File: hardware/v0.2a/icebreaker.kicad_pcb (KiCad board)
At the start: 4 copper layers, 73 x 37 mm, 125 parts, among them J1 Jumper, J10 Jumper, J11 Jumper, J12 Jumper, J13 Jumper, J14 Jumper, J15 Jumper, J16 Jumper, J17 Jumper, J18 Jumper, J19 Jumper, J2 Jumper, J20 Flash, J21 PMOD_1A, J22 PMOD_1B, J23 PMOD_2H, J24 PMOD_2P, J25 RGB Led, J26 5V AUX, J27 5V AUX, J3 Jumper, J4 Jumper, J5 Jumper, J6 Jumper, J7 Jumper, J8 Jumper, J9 Jumper, P1 pkl_USB_OTG, P2 UP, P3 UP, P4 UP, P5 UP, SW1 TACT, SW2 TACT, SW3 TACT, SW4 TACT, U1 93C46B-SOT-23-6, U2 3.3V, U3 1V2, U4 FT2232H, U5 W25Q, U6 ICE5LP4K-SG48, U7 12MHz

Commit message: Minor routing cleanup.
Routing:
- net +5V: track 149.6 -> 147.2 mm
- net /iCE_SCK: track 54.4 -> 55.8 mm
- net /FLASH_~HLD~/~RST~/IO3: track 18.5 -> 17.7 mm, vias 4 -> 3
- net /iCE_SS_B: track 61.7 -> 61.4 mm, vias 6 -> 3

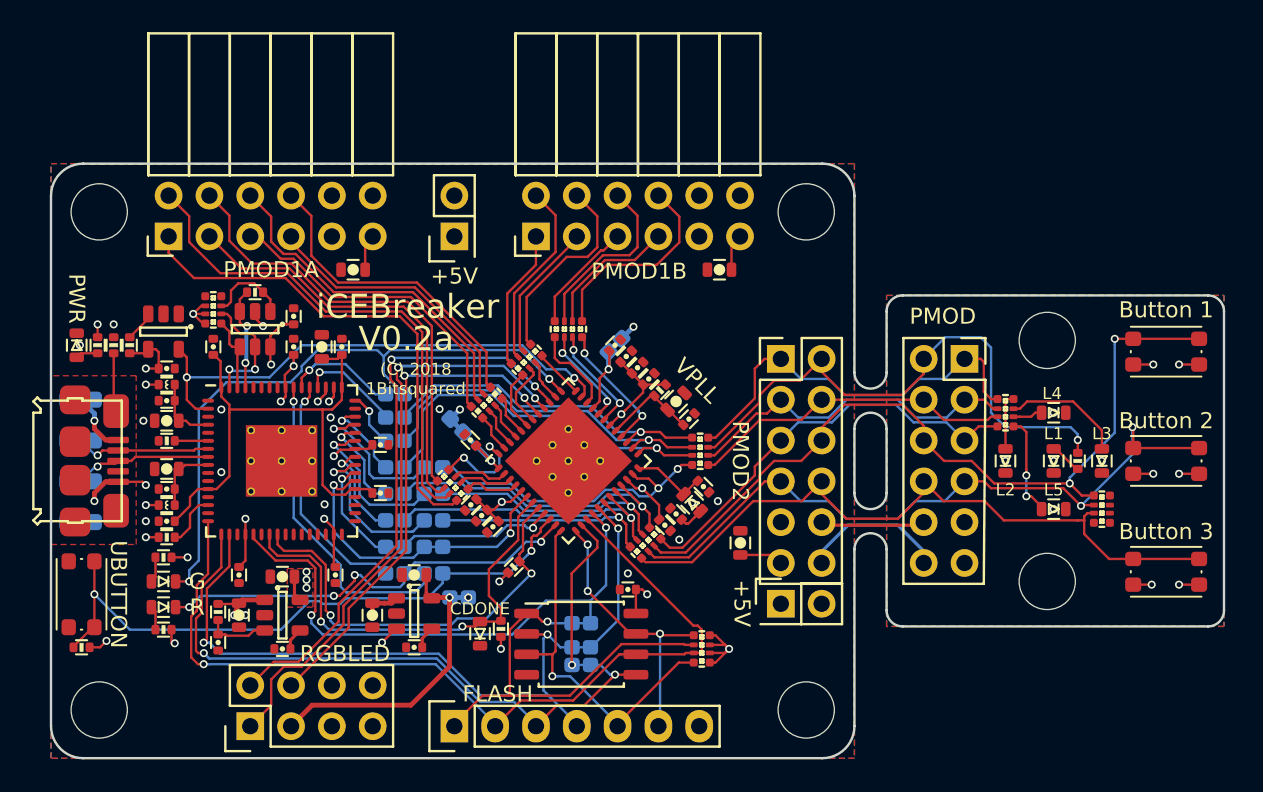
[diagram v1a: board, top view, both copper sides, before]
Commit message: Improved silkscreen legend for more intutive usage.
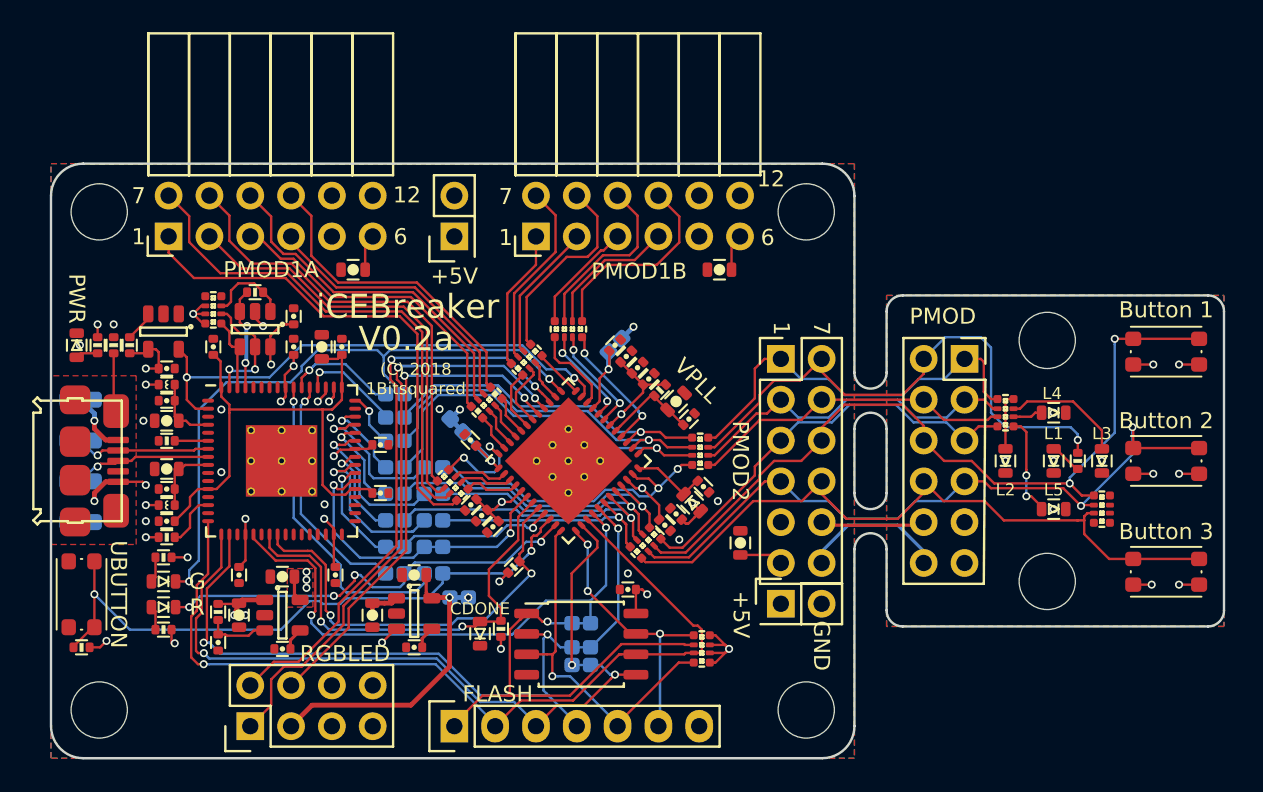
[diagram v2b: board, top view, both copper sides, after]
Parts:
- moved REF** 3.60 mm to (42.2, 47.2)
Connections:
- net Net-(P1-Pad2) renamed /USB_DM
- net Net-(P1-Pad3) renamed /USB_DP
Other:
- board text added: "1"
- board text added: "12"
- board text added: "1B2 (C) 2018 CC-BY-SA 4.0"
- board text added: "3v3"
- board text added: "3v3 5v"
- board text added: "5V"
- board text added: "6"
- board text added: "7"
- board text added: "BLU 1V2"
- board text added: "DM"
- board text added: "DP"
- board text added: "GND"
- board text added: "GND GND"
- board text added: "IO1"
- board text added: "IO2"
- board text added: "IO3"
- board text added: "RED GRN"
- board text added: "SCK"
- board text added: "~CS"

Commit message: Fixed pin header 3d models.
We had some of the models doubled up or not fully disabled. Now the TH
pin headers are all using KiCad V5 3d model locations and are all
disabled.

This fixes #23
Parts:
- removed the REF** at (42.2, 47.2)
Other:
- board text removed: "1Bitsquared"

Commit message: Added more legend silkscreen to ears.
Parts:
- added REF**: 1b2_Logo_SilkS_5mm, pkl_logos:1b2_Logo_SilkS_5mm, B.Cu at (42.2, 47.2)
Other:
- board text added: "1Bitsquared"
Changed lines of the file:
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@@
   (general
     (thickness 1.6)
-    (drawings 142)
+    (drawings 143)
     (tracks 1404)
     (zones 0)
-    (modules 124)
+    (modules 125)
     (nets 125)
   )
@@
     (add_net "Net-(U7-Pad2)")
   )
+  (module pkl_logos:1b2_Logo_SilkS_5mm locked (layer B.Cu)
+    (at 42.2 47.2 180)
+    (fp_text reference REF** (at 0 -4 180) (layer B.Fab) hide
+      (effects (font (size 1 1) (thickness 0.15)) (justify mirror))
+    )
+    (fp_text value 1b2_Logo_SilkS_5mm (at 0 4 180) (layer B.Fab) hide
+      (effects (font (size 1 1) (thickness 0.15)) (justify mirror))
+    )
+    (fp_line (start -0.5 0.5) (end -0.5 2.5) (layer B.SilkS) (width 0.2))
+    (fp_line (start -0.5 2.5) (end -2.5 2.5) (layer B.SilkS) (width 0.2))
+    (fp_line (start -2.5 2.5) (end -2.5 0.5) (layer B.SilkS) (width 0.2))
+    (fp_line (start -2.5 0.5) (end -0.5 0.5) (layer B.SilkS) (width 0.2))
+    (fp_line (start -0.5 2.5) (end 0 2) (layer B.SilkS) (width 0.2))
+    (fp_line (start 0 2) (end 0 0) (layer B.SilkS) (width 0.2))
+    (fp_line (start 0 0) (end -0.5 0.5) (layer B.SilkS) (width 0.2))
+    (fp_line (start -2.5 0.5) (end -2 0) (layer B.SilkS) (width 0.2))
+    (fp_line (start -2 0) (end 0 0) (layer B.SilkS) (width 0.2))
+    (fp_line (start 2 2) (end 0.5 2) (layer B.SilkS) (width 0.2))
+    (fp_line (start 0.5 2) (end 0.5 -0.5) (layer B.SilkS) (width 0.2))
+    (fp_line (start 0.5 -0.5) (end -2 -0.5) (layer B.SilkS) (width 0.2))
+    (fp_line (start -2 -0.5) (end -2 -2) (layer B.SilkS) (width 0.2))
+    (fp_line (start -2 -2) (end 2 -2) (layer B.SilkS) (width 0.2))
+    (fp_line (start 2 -2) (end 2 2) (layer B.SilkS) (width 0.2))
+    (fp_line (start 2 2) (end 2.5 1.5) (layer B.SilkS) (width 0.2))
+    (fp_line (start 2.5 1.5) (end 2.5 -2.5) (layer B.SilkS) (width 0.2))
+    (fp_line (start 2.5 -2.5) (end 2 -2) (layer B.SilkS) (width 0.2))
+    (fp_line (start -2 -2) (end -1.5 -2.5) (layer B.SilkS) (width 0.2))
+    (fp_line (start -1.5 -2.5) (end 2.5 -2.5) (layer B.SilkS) (width 0.2))
+  )
   (module pkl_dipol:R_Array_Convex_4x0402 (layer F.Cu)
     (at 57.105546 43.866206 135)
@@
       (net 1 /Rx_TTL/FIFO_D0))
   )
+  (gr_text 1Bitsquared (at 42.1 51) (layer B.SilkS)
+    (effects (font (size 1 1) (thickness 0.25)) (justify mirror))
+  )
   (gr_text 12 (at 84.3 56.05 270) (layer B.SilkS)

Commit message: Replaced/added the null logo to the boards.
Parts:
- REF**: value 1b2_Logo_SilkS_5mm -> null_Logo_SilkS_5mm; footprint pkl_logos:1b2_Logo_SilkS_5mm -> pkl_logos:null_Logo_SilkS_5mm
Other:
- board text added: "NULL"
- board text removed: "1Bitsquared"
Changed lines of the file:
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@@
-(kicad_pcb (version 20171130) (host pcbnew 5.1.2-f72e74a~84~ubuntu18.04.1)
+(kicad_pcb (version 20171130) (host pcbnew 5.1.5-52549c5~86~ubuntu19.10.1)
   (general
     (thickness 1.6)
@@
     (add_net "Net-(U7-Pad2)")
   )
-  (module pkl_logos:1b2_Logo_SilkS_5mm locked (layer B.Cu)
+  (module pkl_logos:null_Logo_SilkS_5mm locked (layer B.Cu)
     (at 42.2 47.2 180)
     (fp_text reference REF** (at 0 -4 180) (layer B.Fab) hide
       (effects (font (size 1 1) (thickness 0.15)) (justify mirror))
     )
-    (fp_text value 1b2_Logo_SilkS_5mm (at 0 4 180) (layer B.Fab) hide
+    (fp_text value null_Logo_SilkS_5mm (at 0 4 180) (layer B.Fab) hide
       (effects (font (size 1 1) (thickness 0.15)) (justify mirror))
     )
-    (fp_line (start -0.5 0.5) (end -0.5 2.5) (layer B.SilkS) (width 0.2))
-    (fp_line (start -0.5 2.5) (end -2.5 2.5) (layer B.SilkS) (width 0.2))
-    (fp_line (start -2.5 2.5) (end -2.5 0.5) (layer B.SilkS) (width 0.2))
-    (fp_line (start -2.5 0.5) (end -0.5 0.5) (layer B.SilkS) (width 0.2))
-    (fp_line (start -0.5 2.5) (end 0 2) (layer B.SilkS) (width 0.2))
-    (fp_line (start 0 2) (end 0 0) (layer B.SilkS) (width 0.2))
-    (fp_line (start 0 0) (end -0.5 0.5) (layer B.SilkS) (width 0.2))
-    (fp_line (start -2.5 0.5) (end -2 0) (layer B.SilkS) (width 0.2))
-    (fp_line (start -2 0) (end 0 0) (layer B.SilkS) (width 0.2))
-    (fp_line (start 2 2) (end 0.5 2) (layer B.SilkS) (width 0.2))
-    (fp_line (start 0.5 2) (end 0.5 -0.5) (layer B.SilkS) (width 0.2))
-    (fp_line (start 0.5 -0.5) (end -2 -0.5) (layer B.SilkS) (width 0.2))
-    (fp_line (start -2 -0.5) (end -2 -2) (layer B.SilkS) (width 0.2))
-    (fp_line (start -2 -2) (end 2 -2) (layer B.SilkS) (width 0.2))
-    (fp_line (start 2 -2) (end 2 2) (layer B.SilkS) (width 0.2))
-    (fp_line (start 2 2) (end 2.5 1.5) (layer B.SilkS) (width 0.2))
-    (fp_line (start 2.5 1.5) (end 2.5 -2.5) (layer B.SilkS) (width 0.2))
-    (fp_line (start 2.5 -2.5) (end 2 -2) (layer B.SilkS) (width 0.2))
-    (fp_line (start -2 -2) (end -1.5 -2.5) (layer B.SilkS) (width 0.2))
-    (fp_line (start -1.5 -2.5) (end 2.5 -2.5) (layer B.SilkS) (width 0.2))
+    (fp_arc (start -0.4 -0.2) (end -0.7 -0.2) (angle 180) (layer B.SilkS) (width 0.15))
+    (fp_line (start 1 -0.5) (end 1.5 -0.5) (layer B.SilkS) (width 0.15))
+    (fp_line (start 1 0.5) (end 1 -0.5) (layer B.SilkS) (width 0.15))
+    (fp_line (start 0.2 -0.5) (end 0.7 -0.5) (layer B.SilkS) (width 0.15))
+    (fp_line (start 0.2 0.5) (end 0.2 -0.5) (layer B.SilkS) (width 0.15))
+    (fp_line (start -0.1 0.5) (end -0.1 -0.2) (layer B.SilkS) (width 0.15))
+    (fp_line (start -0.7 0.5) (end -0.7 -0.2) (layer B.SilkS) (width 0.15))
+    (fp_line (start -1 -0.5) (end -1 0.5) (layer B.SilkS) (width 0.15))
+    (fp_line (start -1.5 0.5) (end -1 -0.5) (layer B.SilkS) (width 0.15))
+    (fp_line (start -1.5 -0.5) (end -1.5 0.5) (layer B.SilkS) (width 0.15))
+    (fp_line (start 2.5 2.5) (end -2.5 2.5) (layer B.SilkS) (width 0.2))
+    (fp_line (start -2.5 2.5) (end -2.5 -2.5) (layer B.SilkS) (width 0.2))
+    (fp_line (start 2.5 2.5) (end 2.5 -2.5) (layer B.SilkS) (width 0.2))
+    (fp_line (start -2.5 -2.5) (end 2.5 -2.5) (layer B.SilkS) (width 0.2))
   )
   (module pkl_dipol:R_Array_Convex_4x0402 (layer F.Cu)
@@
       (net 1 /Rx_TTL/FIFO_D0))
   )
-  (gr_text 1Bitsquared (at 42.1 51) (layer B.SilkS)
+  (gr_text NULL (at 42.1 51) (layer B.SilkS)
     (effects (font (size 1 1) (thickness 0.25)) (justify mirror))
   )
